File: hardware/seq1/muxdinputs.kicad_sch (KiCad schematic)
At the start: 20 parts, among them SW1 SW_Push, SW2 SW_Push, SW3 SW_Push, SW4 SW_Push, SW5 SW_Push, SW6 SW_Push, SW7 SW_Push, SW8 SW_Push, U2 74HC4051, U3 74HC4051

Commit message: updating the board with new line in
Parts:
- removed SW1, SW2, SW3, SW4, SW5, SW6, SW7, SW8: SW_Push, Button_Switch_THT:SW_PUSH_6mm_H5mm, symbol Switch:SW_Push
- added C18, C19: 1u, Capacitor_THT:C_Disc_D5.0mm_W2.5mm_P2.50mm, symbol Device:C
- added RV12, RV13, RV14, RV15, RV16, RV17, RV18, RV19: 10k, Potentiometer_THT:Potentiometer_Bourns_PTV09A-1_Single_Vertical, symbol Device:R_Potentiometer_US
- added SW1, SW2, SW3, SW4: SW_Push_x4, Adafruit_Trellis:SW_Silicone_Keypad_PushButton_10mm_4x1grid_NH, symbol Adafruit_Trellis:SW_Push_x4
- added TP2, TP3, TP4, TP5: TestPoint, Connector_PinHeader_2.54mm:PinHeader_1x01_P2.54mm_Vertical, symbol Connector:TestPoint
- added U8, U9: 74HC4051, Package_DIP:DIP-16_W7.62mm_Socket, symbol 74xx:74HC4051
- C3, C4: footprint Capacitor_THT:C_Disc_D5.0mm_W2.5mm_P5.00mm -> Capacitor_THT:C_Disc_D5.0mm_W2.5mm_P2.50mm
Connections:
- net +3V3: now also C18.1, C19.1, RV12.1, RV13.1, RV14.1, RV15.1, RV16.1, RV17.1, RV18.1, RV19.1, U8.16 (VCC), U9.16 (VCC)
- net GND: now also C18.2, C19.2, RV12.3, RV13.3, RV14.3, RV15.3, RV16.3, RV17.3, RV18.3, RV19.3, SW1.2, SW1.4, SW1.6, SW1.8, SW2.2, SW2.4, SW2.6, SW2.8, SW3.2, SW3.4, SW3.6, SW3.8, SW4.2, SW4.4, SW4.6, SW4.8, U8.6 (~{E}), U8.7 (VEE), U8.8 (GND), U9.6 (~{E}), U9.7 (VEE), U9.8 (GND)
- net MUX_ADDR0: now also U8.11 (S0), U9.11 (S0)
- net MUX_ADDR1: now also U8.10 (S1), U9.10 (S1)
- net MUX_ADDR2: now also U8.9 (S2), U9.9 (S2)
- net at U2.5 (A5): now also SW2.5
- net at U2.2 (A6): now also SW2.1
- net at RV7.2: now also U3.5 (A5); no longer U3.14 (A1)
- net at U2.12 (A3): now also SW1.5
- net at U2.14 (A1): now also SW1.3
- net at U2.1 (A4): now also SW2.7
- net at U2.13 (A0): now also SW1.1
- net at U2.15 (A2): now also SW1.7
- net at U2.4 (A7): now also SW2.3
- net at RV2.2: now also U3.14 (A1); no longer U3.5 (A5)
- net at U3.1 (A4): now also RV8.2; no longer RV1.2
- net at U3.12 (A3): now also RV3.2; no longer RV6.2
- net at U3.13 (A0): now also RV1.2; no longer RV8.2
- net at U3.15 (A2): now also RV4.2; no longer RV5.2
- net at U3.2 (A6): now also RV5.2; no longer RV4.2
- net at U3.4 (A7): now also RV6.2; no longer RV3.2
- net POT_MUX renamed POT_MUX_A
- net POT_MUX_A: now also TP3.1
- net SW_MUX renamed SW_MUX_A
- net SW_MUX_A: now also TP2.1
- new net: SW3.5, U8.12 (A3)
- new net: RV16.2, U9.2 (A6)
- new net: RV19.2, U9.1 (A4)
- new net: RV14.2, U9.12 (A3)
- new net: RV12.2, U9.13 (A0)
- new net: RV13.2, U9.14 (A1)
- new net: RV15.2, U9.15 (A2)
- new net: RV17.2, U9.4 (A7)
- new net: RV18.2, U9.5 (A5)
- new net: SW4.1, U8.2 (A6)
- new net: SW4.3, U8.4 (A7)
- new net: SW4.7, U8.1 (A4)
- new net: SW3.1, U8.13 (A0)
- new net: SW4.5, U8.5 (A5)
- new net: SW3.3, U8.14 (A1)
- new net: SW3.7, U8.15 (A2)
- new net POT_MUX_B: TP5.1, U9.3 (A)
- new net SW_MUX_B: TP4.1, U8.3 (A)
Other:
- company: (none) -> idyllm
- title: (none) -> Sequencer
- moved on the sheet: C3, C4, RV1, RV2, RV3, RV4, RV5, RV6, RV7, RV8, U2, U3

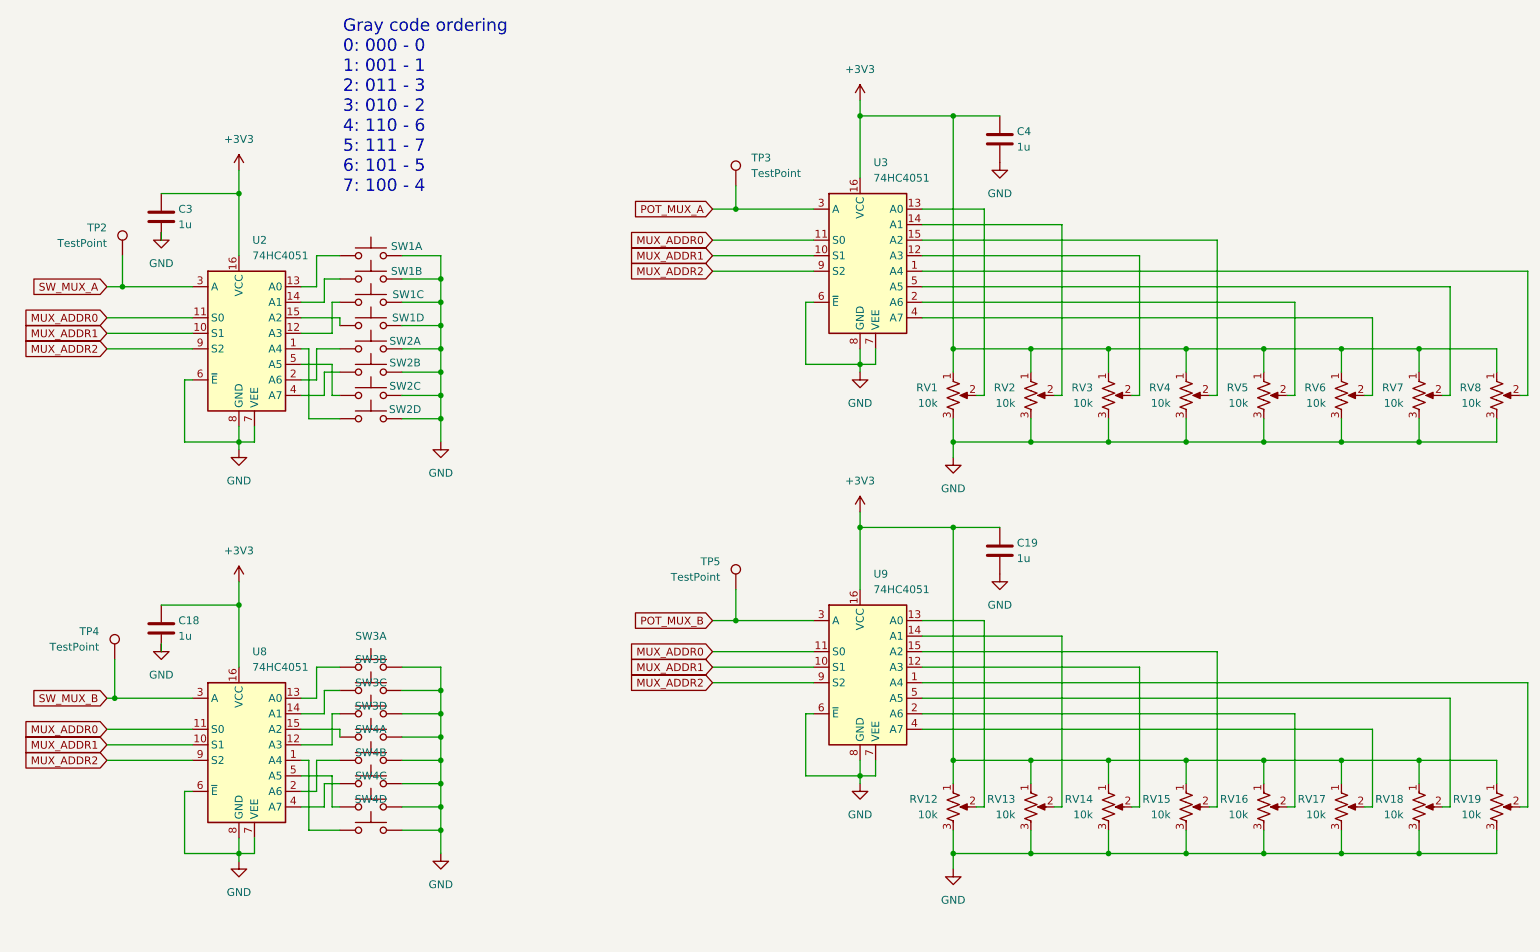
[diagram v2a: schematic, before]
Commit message: layout for v2 board (WIP) with risers part of same schematic/PBC
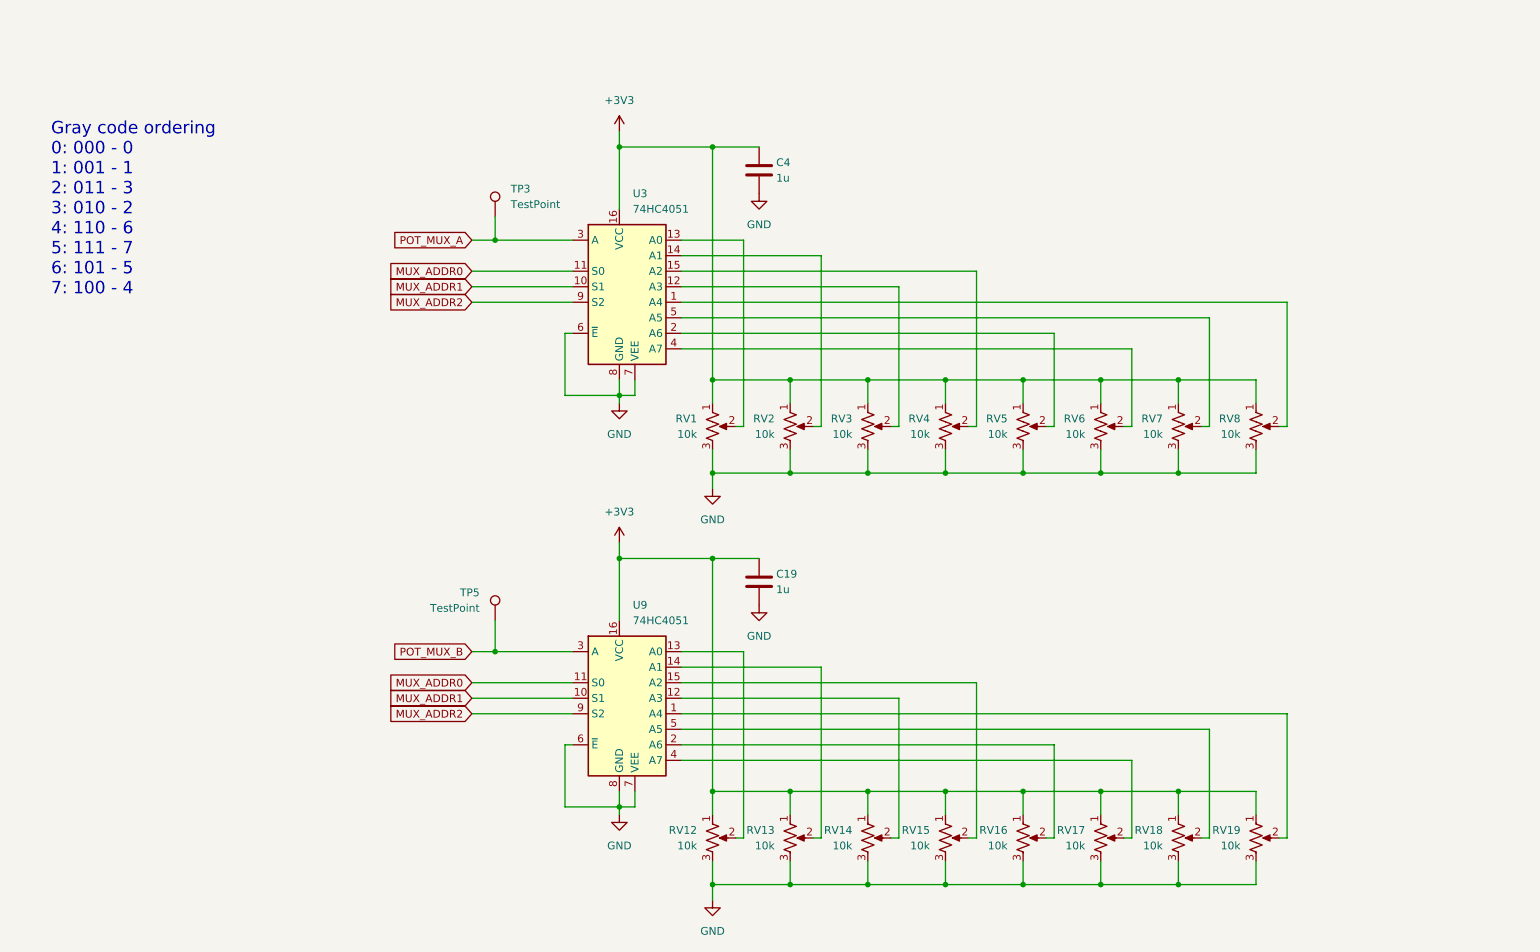
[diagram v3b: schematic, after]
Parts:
- removed C18, C3: 1u, Capacitor_THT:C_Disc_D5.0mm_W2.5mm_P2.50mm, symbol Device:C
- removed SW1, SW2, SW3, SW4: SW_Push_x4, Adafruit_Trellis:SW_Silicone_Keypad_PushButton_10mm_4x1grid_NH, symbol Adafruit_Trellis:SW_Push_x4
- removed TP2, TP4: TestPoint, Connector_PinHeader_2.54mm:PinHeader_1x01_P2.54mm_Vertical, symbol Connector:TestPoint
- removed U2, U8: 74HC4051, Package_DIP:DIP-16_W7.62mm_Socket, symbol 74xx:74HC4051
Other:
- moved on the sheet: C19, C4, RV1, RV12, RV13, RV14, RV15, RV16, RV17, RV18, RV19, RV2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
